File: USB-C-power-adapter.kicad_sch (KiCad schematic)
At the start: 0 parts

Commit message: [#57006] Add USB-C connector
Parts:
- added D1: PESD5V0U1BB, antmicro-footprints:SOD-523, symbol antmicroTVSDiodes:PESD5V0U1BB
- added F1: F_5A_2920, antmicro-footprints:2920-fuse, symbol antmicroFuses:F_5A_2920
- added J1: USB-C_GCT_USB4105-GF-A, antmicro-footprints:USB-C_Receptacle_GCT_USB4105-GF-A, symbol antmicroUSBConnectors:USB-C_GCT_USB4105-GF-A
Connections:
- new net: D1.1, F1.1, J1.A4 (VBUS), J1.A9 (VBUS), J1.B4 (VBUS), J1.B9 (VBUS)
- new net GND: D1.2, J1.A1 (GND), J1.A12 (GND), J1.B1 (GND), J1.B12 (GND), J1.SH
- new net USB.CC1: J1.A5 (CC_{1})
- new net USB.CC2: J1.B5 (CC_{2})
- new net VBUS: F1.2
- no-connect marks 0 -> 6
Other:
- note added: "USB-C PD Input"

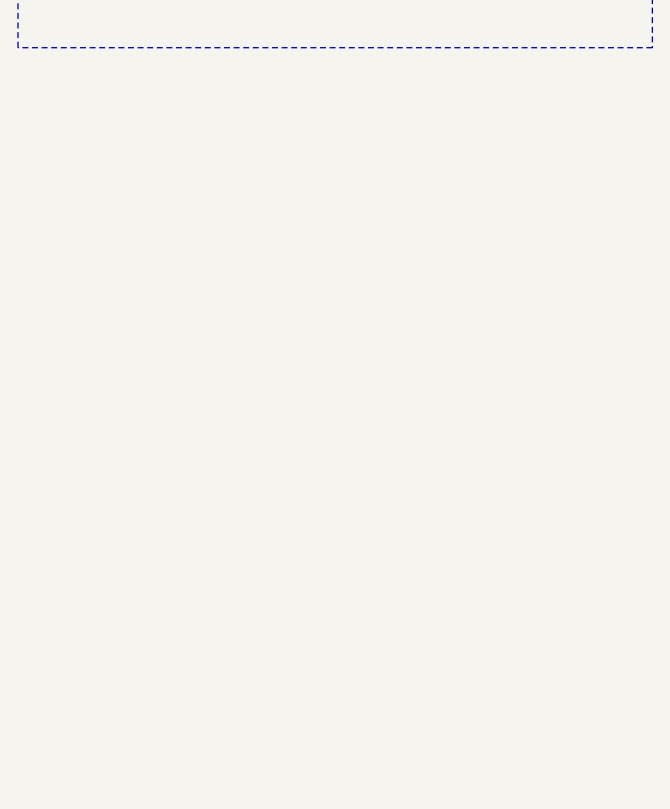
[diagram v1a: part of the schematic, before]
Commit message: [#57006] Add qwiic connector
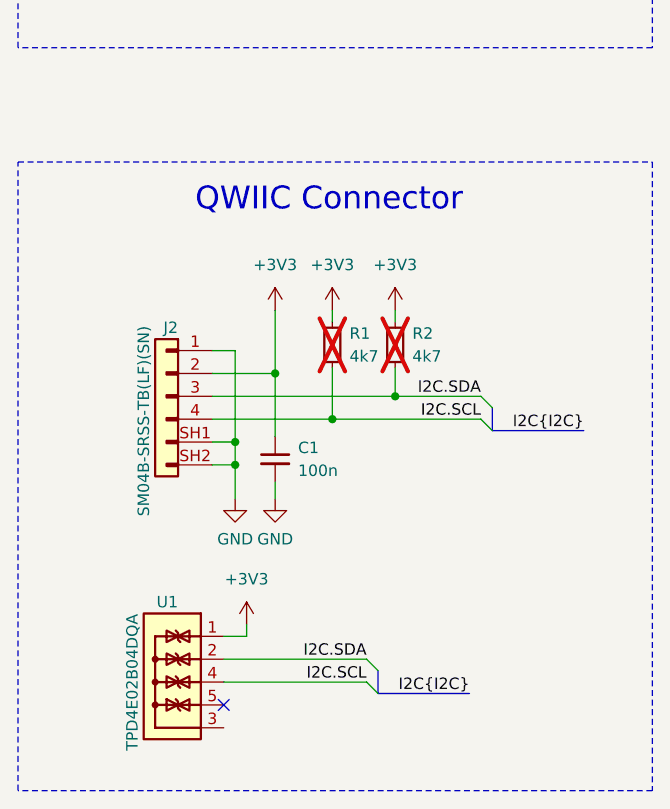
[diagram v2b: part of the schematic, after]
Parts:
- added C1: C_100n_16V_X7R_0402, antmicro-footprints:C_0402_1005Metric, symbol antmicroCapacitors0402:C_100n_16V_X7R_0402
- added J2: JST_SH_1x4_SM04B-SRSS-TB-LF-SN, antmicro-footprints:Conn_JST_SH_1x4_SM04B-SRSS-TB-LF-SN, symbol antmicroWire2BoardConnectors:JST_SH_1x4_SM04B-SRSS-TB-LF-SN
- added R1, R2: R_4k7_0402, antmicro-footprints:R_0402_1005Metric, symbol antmicroResistors0402:R_4k7_0402
- added U1: TPD4E02B04DQA, antmicro-footprints:USON-10_2.5x1mm_P0.5mm, symbol antmicroTVSDiodes:TPD4E02B04DQA
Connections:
- net GND: now also C1.2, J2.1, J2.SH1, J2.SH2
- new net: U1.3, U1.8
- new net: U1.5, U1.6
- new net +3V3: C1.1, J2.2, R1.2, R2.2, U1.1, U1.10
- new net I2C.SCL: J2.4, R1.1, U1.4, U1.7
- new net I2C.SDA: J2.3, R2.1, U1.2, U1.9
- no-connect marks 6 -> 7
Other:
- note added: "QWIIC Connector"

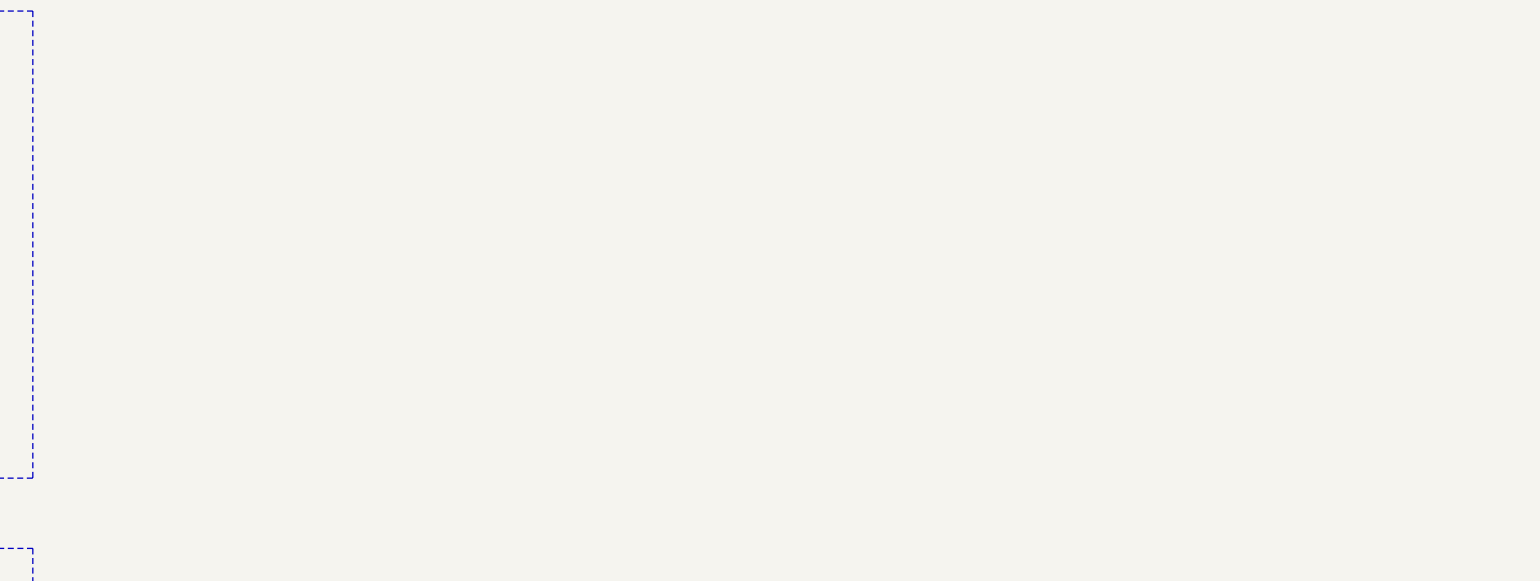
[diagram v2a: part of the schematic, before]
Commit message: [#57006] Add Buck converter
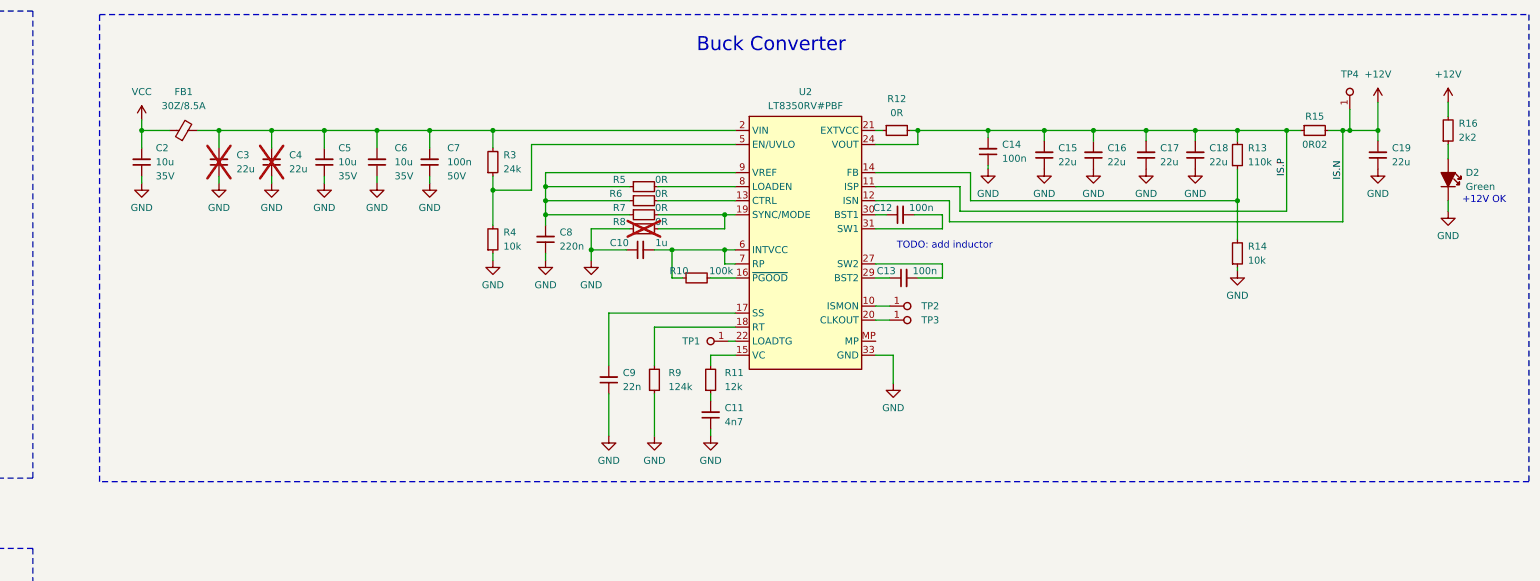
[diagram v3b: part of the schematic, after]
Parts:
- added C10: C_1u_0402, antmicro-footprints:C_0402_1005Metric, symbol antmicroCapacitors0402:C_1u_0402
- added C11: C_4n7_0402, antmicro-footprints:C_0402_1005Metric, symbol antmicroCapacitors0402:C_4n7_0402
- added C12, C13, C14: C_100n_0402, antmicro-footprints:C_0402_1005Metric, symbol antmicroCapacitors0402:C_100n_0402
- added C15, C16, C17, C18, C19: C_22u_16V_0603, antmicro-footprints:C_0603_1608Metric, symbol antmicroCapacitors0603:C_22u_16V_0603
- added C2, C5, C6: C_10u_0805_35V, antmicro-footprints:C_0805_2012Metric, symbol antmicroCapacitorsmisc:C_10u_0805_35V
- added C3, C4: C_22u_1206_35V, antmicro-footprints:C_1206_3216Metric, symbol antmicroCapacitorsmisc:C_22u_1206_35V
- added C7: C_100n_50V_X8L_0402, antmicro-footprints:C_0402_1005Metric, symbol antmicroCapacitors0402:C_100n_50V_X8L_0402
- added C8: C_220n_6V3_X7R_0402, antmicro-footprints:C_0402_1005Metric, symbol antmicroCapacitors0402:C_220n_6V3_X7R_0402
- added C9: C_22n_0402, antmicro-footprints:C_0402_1005Metric, symbol antmicroCapacitors0402:C_22n_0402
- added D2: LED_G_0603_LG_L29K-G2J1-24-Z, antmicro-footprints:LED_0603_1608Metric_G, symbol antmicroLEDIndicationDiscrete:LED_G_0603_LG_L29K-G2J1-24-Z
- added FB1: FB_30Z_8.5A_Murata-BLM21SN_0805, antmicro-footprints:FB_0805_2012Metric, symbol antmicroFerriteBeadsandChips:FB_30Z_8.5A_Murata-BLM21SN_0805
- added R10: R_100k_0402, antmicro-footprints:R_0402_1005Metric, symbol antmicroResistors0402:R_100k_0402
- added R11: R_12k_0402, antmicro-footprints:R_0402_1005Metric, symbol antmicroResistors0402:R_12k_0402
- added R12, R5, R6, R7, R8: R_0R_0402, antmicro-footprints:R_0402_1005Metric, symbol antmicroResistors0402:R_0R_0402
- added R13: R_110k_0402, antmicro-footprints:R_0402_1005Metric, symbol antmicroResistors0402:R_110k_0402
- added R14, R4: R_10k_0402, antmicro-footprints:R_0402_1005Metric, symbol antmicroResistors0402:R_10k_0402
- added R15: R_0R02_1206, thunderbolt-gpu-adapter-footprints:R_1206_3216Metric, symbol thunderbolt-gpu-adapter:R_0R02_1206
- added R16: R_2k2_0402, antmicro-footprints:R_0402_1005Metric, symbol antmicroResistors0402:R_2k2_0402
- added R3: R_24k_0402, antmicro-footprints:R_0402_1005Metric, symbol antmicroResistors0402:R_24k_0402
- added R9: R_124k_0402, antmicro-footprints:R_0402_1005Metric, symbol antmicroResistors0402:R_124k_0402
- added TP1, TP2, TP3, TP4: TP_0.75mm_SMD, antmicro-footprints:TP_SMD_0.75mm, symbol antmicroTestPoints:TP_0.75mm_SMD
- added U2: LT8350RV, antmicro-footprints:QFN-32-4EP_4x6mm_P0.5mm, symbol antmicroDCDCConverters:LT8350RV
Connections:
- net GND: now also C10.1, C11.1, C14.1, C15.1, C16.1, C17.1, C18.1, C19.1, C2.1, C3.1, C4.1, C5.1, C6.1, C7.1, C8.1, C9.1, D2.2, R14.1, R4.1, R8.1, R9.1, U2.33 (GND), U2.34 (GND), U2.35 (GND), U2.36 (GND)
- new net: C3.2, C4.2, C5.2, C6.2, C7.2, FB1.2, R3.2, U2.2 (VIN), U2.3 (VIN)
- new net: R3.1, R4.2, U2.5 (EN/UVLO)
- new net: C8.2, R5.1, R6.1, R7.1, U2.9 (VREF)
- new net: R7.2, R8.2, U2.19 (SYNC/MODE)
- new net: C11.2, R11.1
- new net: R11.2, U2.15 (VC)
- new net: R9.2, U2.18 (RT)
- new net: C10.2, R10.1, U2.6 (INTVCC), U2.7 (RP)
- new net: C12.1, U2.30 (BST1)
- new net: C12.2, U2.31 (SW1), U2.32 (SW1)
- new net: TP2.1, U2.10 (ISMON)
- new net: R6.2, U2.13 (CTRL)
- new net: R13.1, R14.2, U2.14 (FB)
- new net: R10.2, U2.16 (~{PGOOD})
- new net: C9.2, U2.17 (SS)
- new net: TP3.1, U2.20 (CLKOUT)
- new net: R12.1, U2.21 (EXTVCC)
- new net: TP1.1, U2.22 (LOADTG)
- new net: C13.2, U2.27 (SW2), U2.28 (SW2)
- new net: C13.1, U2.29 (BST2)
- new net: R5.2, U2.8 (LOADEN)
- new net: D2.1, R16.1
- new net +12V: C19.2, R15.2, R16.2, TP4.1, U2.12 (ISN)
- new net IS.P: C14.2, C15.2, C16.2, C17.2, C18.2, R12.2, R13.2, R15.1, U2.11 (ISP), U2.24 (VOUT), U2.25 (VOUT)
- new net VCC: C2.2, FB1.1
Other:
- note added: "+12V OK"
- note added: "Buck Converter"
- note added: "TODO: add inductor"

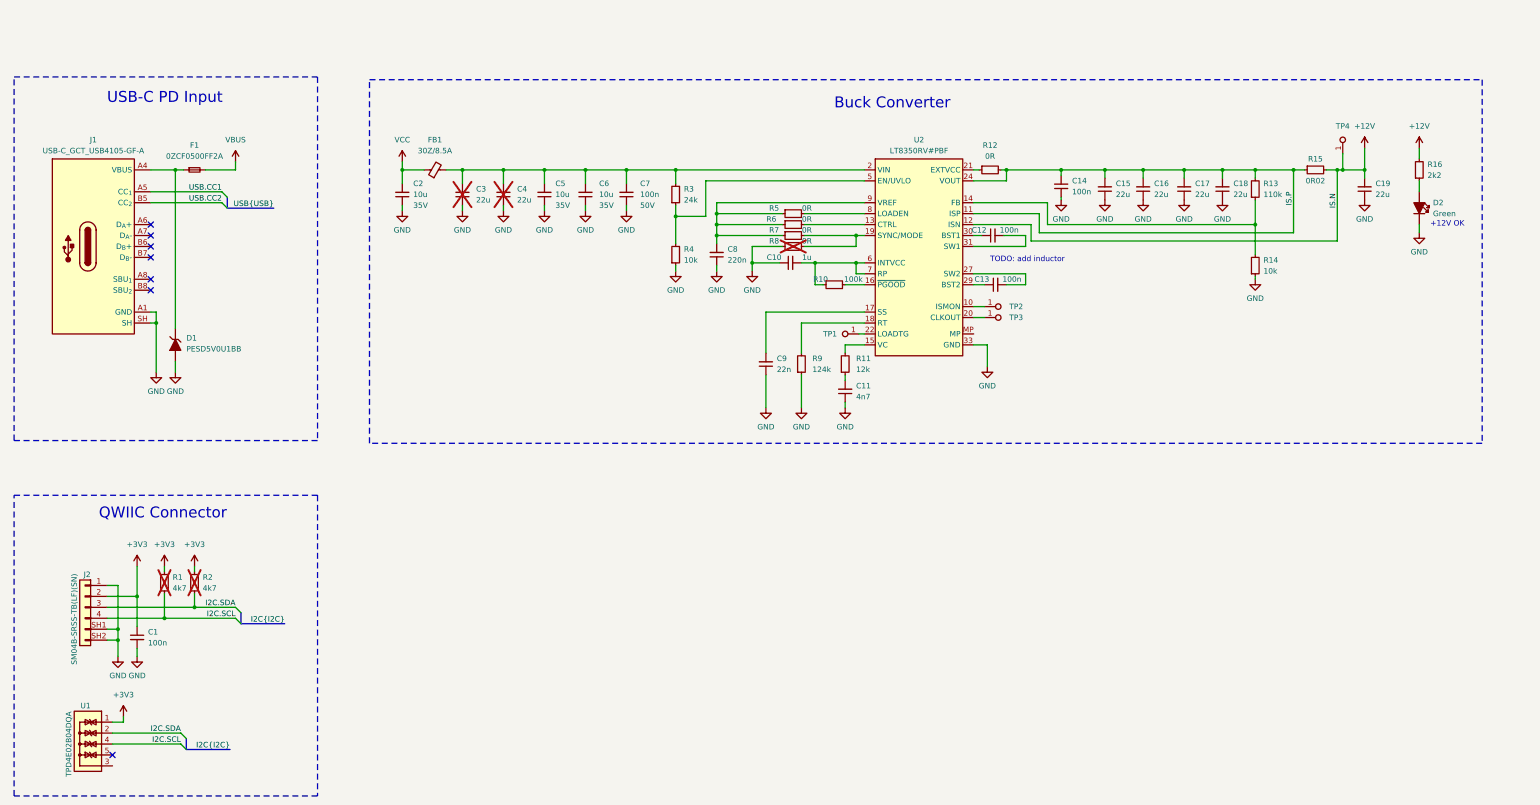
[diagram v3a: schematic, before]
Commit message: [#57006] Add USB PD controller
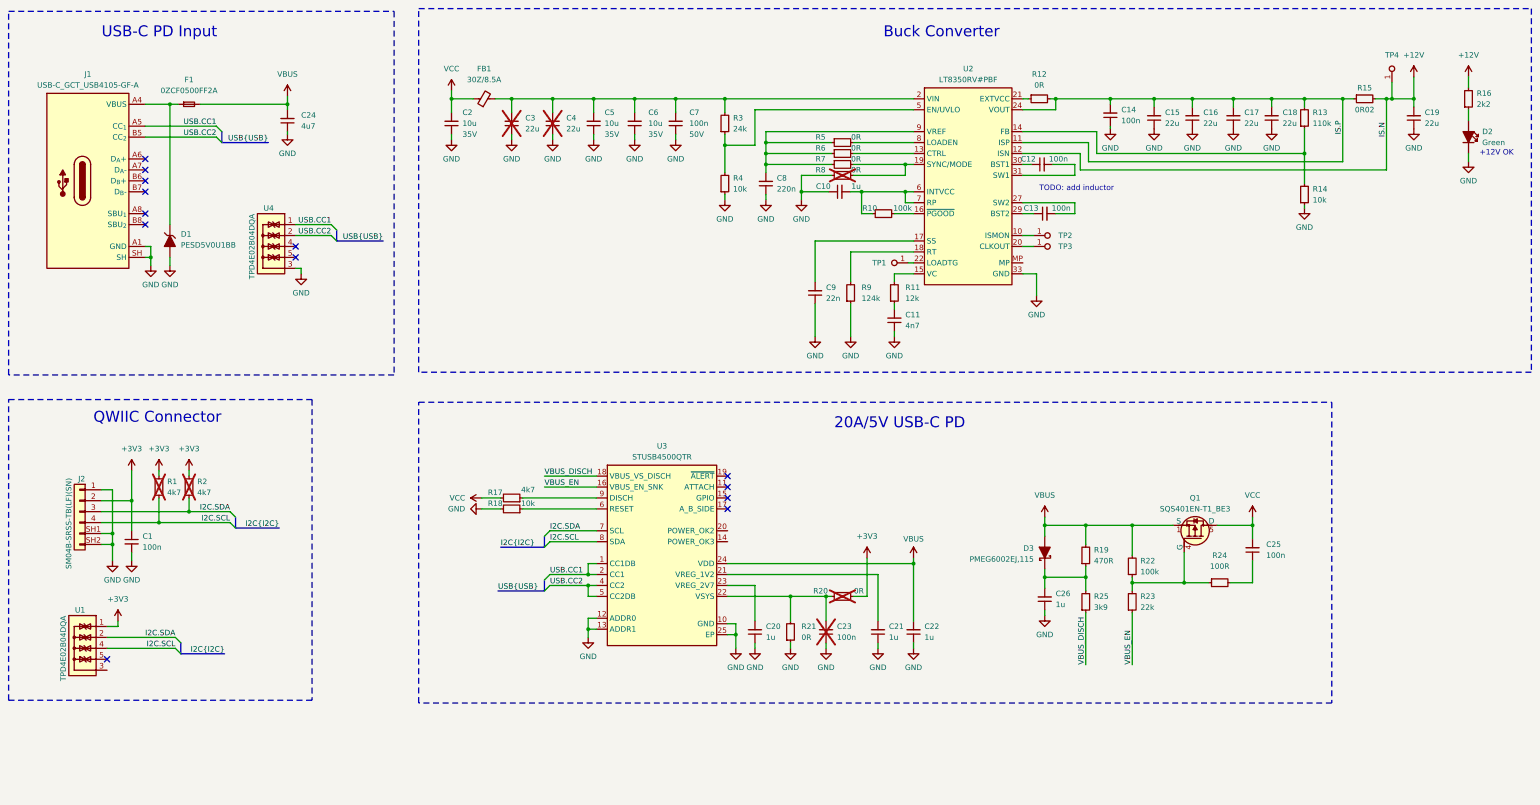
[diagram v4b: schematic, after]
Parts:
- added C20, C21, C22, C26: C_1u_0402, antmicro-footprints:C_0402_1005Metric, symbol antmicroCapacitors0402:C_1u_0402
- added C23: C_100n_0402, antmicro-footprints:C_0402_1005Metric, symbol antmicroCapacitors0402:C_100n_0402
- added C24: C_4u7_25V_0402, antmicro-footprints:C_0402_1005Metric, symbol antmicroCapacitors0402:C_4u7_25V_0402
- added C25: C_100n_50V_X8L_0402, antmicro-footprints:C_0402_1005Metric, symbol antmicroCapacitors0402:C_100n_50V_X8L_0402
- added D3: PMEG6002EJ,115, antmicro-footprints:D_SOD-323F, symbol antmicroDiodesRectifiersSingle:PMEG6002EJ,115
- added Q1: SQS401EN-T1_BE3, antmicro-footprints:Vishay_PowerPAK_1212-8_Single, symbol antmicroTransistorsFETsMOSFETsSingle:SQS401EN-T1_BE3
- added R17: R_4k7_0805, antmicro-footprints:R_0805_2012Metric, symbol antmicroResistorsmisc:R_4k7_0805
- added R18: R_10k_0402, antmicro-footprints:R_0402_1005Metric, symbol antmicroResistors0402:R_10k_0402
- added R19: R_470R_0603, antmicro-footprints:R_0603_1608Metric, symbol antmicroResistors0603:R_470R_0603
- added R20, R21: R_0R_0402, antmicro-footprints:R_0402_1005Metric, symbol antmicroResistors0402:R_0R_0402
- added R22: R_100k_0402, antmicro-footprints:R_0402_1005Metric, symbol antmicroResistors0402:R_100k_0402
- added R23: R_22k_0402, antmicro-footprints:R_0402_1005Metric, symbol antmicroResistors0402:R_22k_0402
- added R24: R_100R_0402, antmicro-footprints:R_0402_1005Metric, symbol antmicroResistors0402:R_100R_0402
- added R25: R_3k9_0603, antmicro-footprints:R_0603_1608Metric, symbol antmicroResistors0603:R_3k9_0603
- added U3: STUSB4500_QFN, antmicro-footprints:QFN-24-1EP_4x4mm_P0.5_EP2.1x2.1mm, symbol antmicroPMICPowerDistributionSwitchesLoadDrivers:STUSB4500_QFN
- added U4: TPD4E02B04DQA, antmicro-footprints:USON-10_2.5x1mm_P0.5mm, symbol antmicroTVSDiodes:TPD4E02B04DQA
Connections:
- net +3V3: now also R20.2
- net GND: now also C20.1, C21.1, C22.1, C23.1, C24.1, C26.1, R18.2, R21.1, U3.10 (GND), U3.12 (ADDR0), U3.13 (ADDR1), U3.25 (EP), U4.3, U4.8
- net I2C.SCL: now also U3.8 (SDA)
- net I2C.SDA: now also U3.7 (SCL)
- net USB.CC1: now also U3.1 (CC1DB), U3.2 (CC1), U4.1, U4.10
- net USB.CC2: now also U3.4 (CC2), U3.5 (CC2DB), U4.2, U4.9
- net VBUS: now also C22.2, C24.2, D3.A, Q1.1 (S), Q1.2 (S), Q1.3 (S), R19.2, R22.2, U3.24 (VDD)
- net VCC: now also C25.2, Q1.5 (D), R17.2
- new net: Q1.4 (G), R22.1, R23.2, R24.1
- new net: C26.2, D3.K, R19.1, R25.2
- new net: R17.1, U3.9 (DISCH)
- new net: U4.4, U4.7
- new net: U4.5, U4.6
- new net: C23.2, R20.1, R21.2, U3.22 (VSYS)
- new net: C21.2, U3.21 (VREG_1V2)
- new net: C20.2, U3.23 (VREG_2V7)
- new net: R18.1, U3.6 (RESET)
- new net: C25.1, R24.2
- new net VBUS_DISCH: R25.1, U3.18 (VBUS_VS_DISCH)
- new net VBUS_EN: R23.1, U3.16 (VBUS_EN_SNK)
- no-connect marks 7 -> 13
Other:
- note added: "20A/5V USB-C PD"
- moved on the sheet: C1, C10, C11, C12, C13, C14, C15, C16, C17, C18, C19, C2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

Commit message: [#57006] Update schematic
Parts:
- removed D1: PESD5V0U1BB, antmicro-footprints:SOD-523, symbol antmicroTVSDiodes:PESD5V0U1BB
- added F2: F_7A_1206, antmicro-footprints:F_1206_3216Metric, symbol antmicroFuses:F_7A_1206
- added J3: Conn_Molex_NanoFit_1053131202, thunderbolt-gpu-adapter-footprints:Conn_Molex_NanoFit_1053131202, symbol thunderbolt-gpu-adapter:Conn_Molex_NanoFit_1053131202
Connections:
- net +12V: now also F2.1
- net GND: now also J3.2
- net USB.CC1: now also U4.2, U4.9; no longer U4.1, U4.10
- net USB.CC2: now also U4.4, U4.7; no longer U4.2, U4.9
- net VBUS: now also U4.1, U4.10
- new net: F2.2, J3.1
- no-connect marks 13 -> 12
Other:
- note added: "USB-C PD Controller"
- note removed: "20A/5V USB-C PD"
- moved on the sheet: D2, R16, U4
